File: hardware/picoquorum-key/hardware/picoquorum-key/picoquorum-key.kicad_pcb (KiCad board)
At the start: 2 copper layers, 44 x 53 mm, 52 parts, among them J1 USB-C, J2 ST7789 1.14in panel, Q1 AO3401A, Q2 MMBT3904, SW1 D0 Reject, SW2 D1 Next, SW3 D2 Sign, SW6 BOOT, SW7 RESET, U1 ESP32-S3-WROOM-1-N8R2, U2 ATECC608C-MAHDA, U3 AMS1117-3.3, U4 USBLC6-2SC6

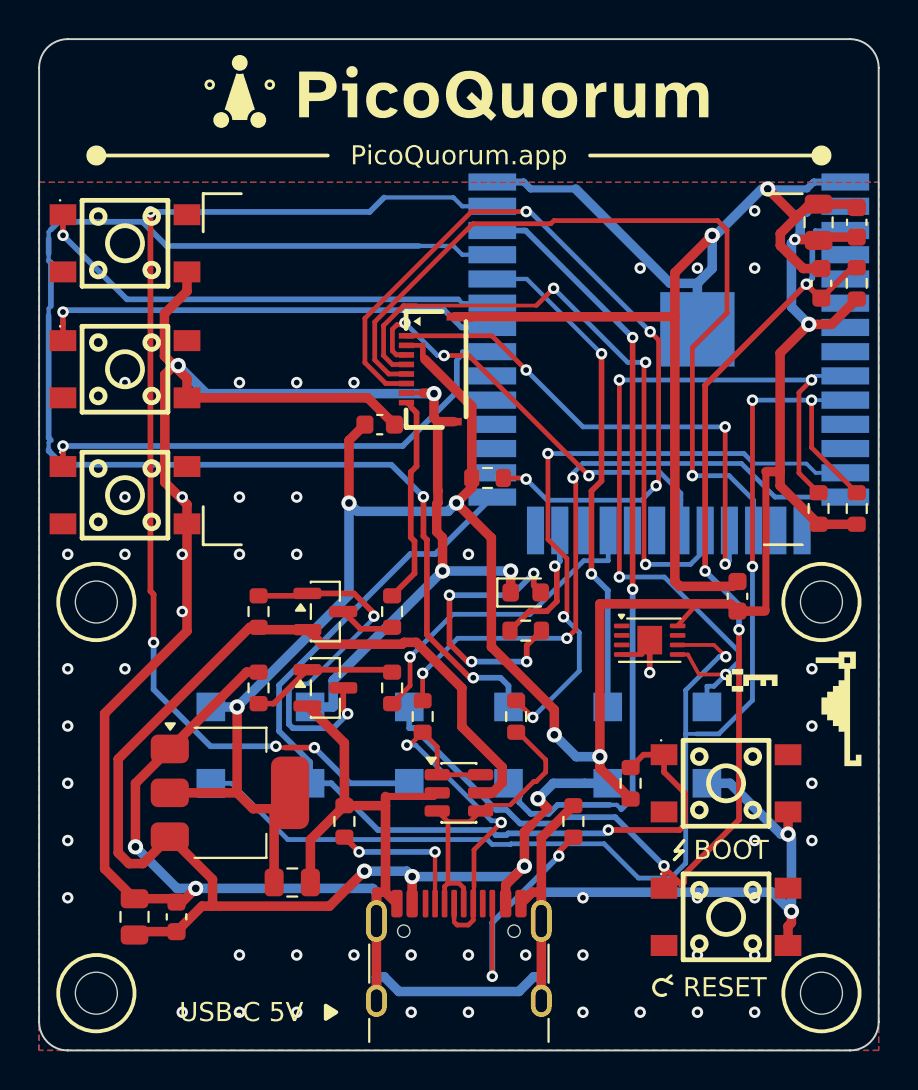
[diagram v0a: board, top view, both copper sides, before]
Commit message: picoquorum-key: an optional key port, a right-angle USB-C plug for key-c
Pads on the back for an HRO TYPE-C-31-G-03 plug at the left edge, beside the
module, its body past the edge, and its parts beside it: an AP22653 switch for
the key's power (80 mA, reverse blocking, IO2 enables it), SRV05-4 ESD on SDA,
SCL and CC, a TVS on VKEY, 2.2k pull-ups to VKEY, and CC on IO1 through a 22k
pull-up, so a key in reads 0.62 V (a logic low) and a swap shows as two edges.
The plugged key gets its own bus, IO39/IO38, since it and U2 both answer at
0x60.

Every port part is DNP: bom.csv and cpl.csv are byte for byte as before, and
unfitted the board behaves as rev A did. The console image doesn't use the port
yet; that is a firmware change and a new release.

The plug's escape is drawn and locked by gen_pcb.py. The board was routed
again (DESIGN.md, Routing): DRC, ERC and parity clean, USB skew 8.7 mm.
post_route.py no longer stacks a stitching via on an existing one. The back's
title text moved to make room. tools/test.sh: 125 tests pass, 11 skipped (no
FreeCAD here); golden images re-approved after checking the diffs.

Co-Authored-By: Claude Opus 5.5 <noreply@anthropic.com>
Claude-Session: https://claude.ai/code/session_01F8ny43JrASLAVMDnk3ynk2
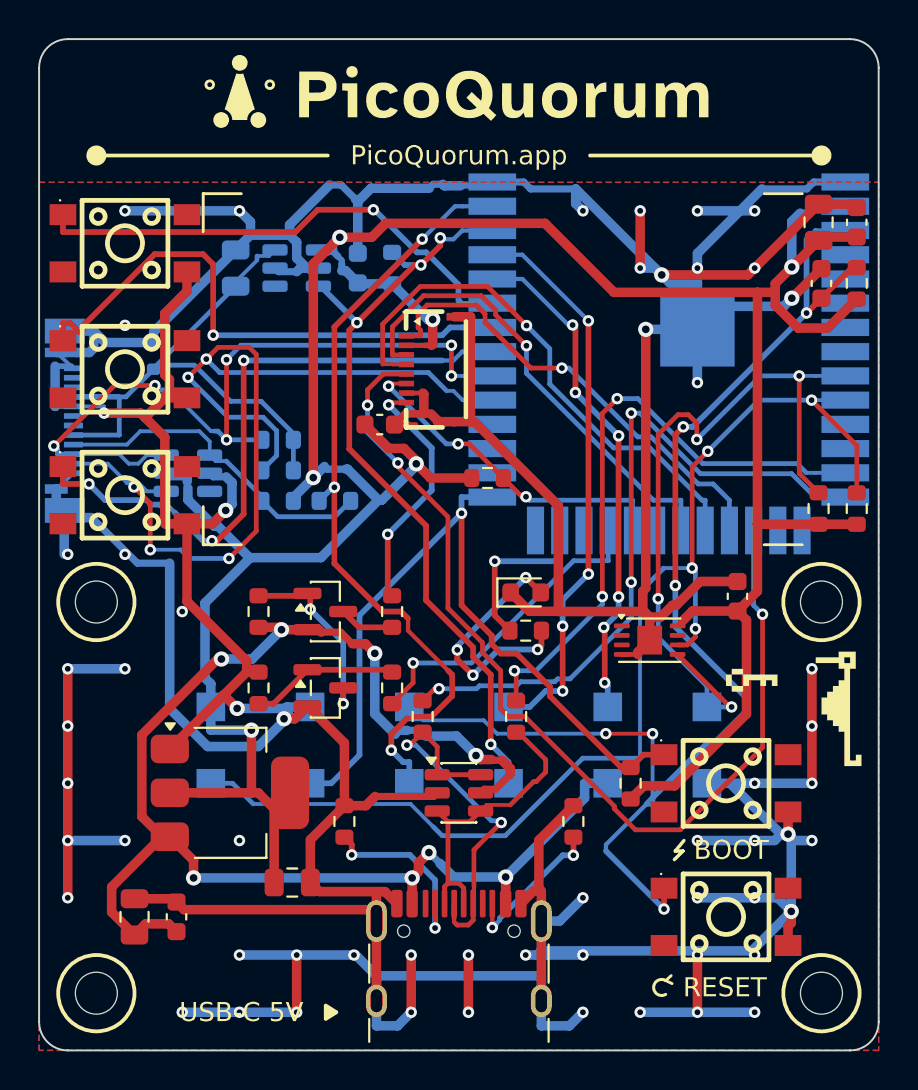
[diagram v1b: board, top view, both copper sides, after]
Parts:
- added C10: 10u, Capacitor_SMD:C_0805_2012Metric, B.Cu at (110.3, 72.0)
- added C9: 100n, Capacitor_SMD:C_0603_1608Metric, B.Cu at (116.7, 72.0)
- added D2: ESD5Z5V0, Diode_SMD:D_SOD-523, B.Cu at (106.0, 76.6)
- added J3: USB-C plug, console:USB_C_Plug_HRO_TYPE-C-31-G-03_Edge, B.Cu at (100.0, 80.0)
- added R15: 2.2k, Resistor_SMD:R_0603_1608Metric, B.Cu at (112.5, 81.0)
- added R16: 2.2k, Resistor_SMD:R_0603_1608Metric, B.Cu at (112.5, 82.6)
- added R17: 22k, Resistor_SMD:R_0603_1608Metric, B.Cu at (112.5, 84.2)
- added R18: 1k, Resistor_SMD:R_0603_1608Metric, B.Cu at (115.5, 84.2)
- added R19: 10k, Resistor_SMD:R_0603_1608Metric, B.Cu at (118.5, 72.0)
- added U5: AP22653W6-7, Package_TO_SOT_SMD:SOT-23-6, B.Cu at (113.5, 72.0)
- added U6: SRV05-4, Package_TO_SOT_SMD:SOT-23-6, B.Cu at (107.8, 82.8)
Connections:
- U1 pad 31: unconnected-(U1-IO38-Pad31) -> KEY_SCL
- U1 pad 32: unconnected-(U1-IO39-Pad32) -> KEY_SDA
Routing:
- net GND: track 274.5 -> 418.7 mm, vias 62 -> 59
- net KEY_SCL: track 0.00 -> 53.6 mm, vias 0 -> 5
- net UART_TX: track 70.3 -> 29.6 mm, vias 2 -> 4
- net KEY_SDA: track 0.00 -> 40.0 mm, vias 0 -> 6
- net +3V3: track 126.5 -> 162.8 mm, vias 7 -> 6
- net VKEY: track 0.00 -> 31.8 mm
- net LCD_RST: track 43.5 -> 17.8 mm, vias 4 -> 3
- net KEY_CC: track 0.00 -> 17.6 mm
- net IO1: track 59.0 -> 41.6 mm, vias 4 -> 3
- net I2C_SCL: track 72.6 -> 62.9 mm
- net BL_GATE: track 19.5 -> 10.0 mm
- net LCD_DC: track 43.8 -> 51.8 mm, vias 1 -> 3
- net BOOT: track 48.2 -> 40.4 mm
- net BTN_SIGN: track 26.7 -> 33.5 mm, vias 1 -> 3
- net LCD_MOSI: track 34.2 -> 28.4 mm, vias 3 -> 1
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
